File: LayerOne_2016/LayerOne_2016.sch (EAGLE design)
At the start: 63 parts, among them IC1 M74VHC1GT125DF2G, IC2 PQ1X331M2ZP-3V3-LDO-SOT-23-5, IC9 M74VHC1GT125DF2G

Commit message: 
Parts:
- added JP10, JP6, JP7, JP8, JP9: (no value), SparkFun-Connectors:PINHD-2X10
- added JP11, JP12, JP13: (no value), microbuilder:HEADER-1X10
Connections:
- net 3.3V: now also JP11.1, JP11.10, JP11.2, JP11.3, JP11.4, JP11.5, JP11.6, JP11.7, JP11.8, JP11.9
- net GND: now also JP12.1, JP12.10, JP12.2, JP12.3, JP12.4, JP12.5, JP12.6, JP12.7, JP12.8, JP12.9
- net VCC: now also JP13.1, JP13.10, JP13.2, JP13.3, JP13.4, JP13.5, JP13.6, JP13.7, JP13.8, JP13.9
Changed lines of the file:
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@@
 </part>
 <part name="GND13" library="SparkFun-Aesthetics" deviceset="GND" device=""/>
+<part name="JP6" library="SparkFun-Connectors" deviceset="PINHD-2X10" device=""/>
+<part name="JP7" library="SparkFun-Connectors" deviceset="PINHD-2X10" device=""/>
+<part name="JP8" library="SparkFun-Connectors" deviceset="PINHD-2X10" device=""/>
+<part name="JP9" library="SparkFun-Connectors" deviceset="PINHD-2X10" device=""/>
+<part name="JP10" library="SparkFun-Connectors" deviceset="PINHD-2X10" device=""/>
+<part name="JP11" library="microbuilder" deviceset="HEADER-1X10" device=""/>
+<part name="JP12" library="microbuilder" deviceset="HEADER-1X10" device=""/>
+<part name="JP13" library="microbuilder" deviceset="HEADER-1X10" device=""/>
+<part name="U$2" library="microbuilder" deviceset="GND" device=""/>
 </parts>
 <sheets>
@@
 </plain>
 <instances>
+<instance part="JP6" gate="A" x="-10.16" y="66.04"/>
+<instance part="JP7" gate="A" x="7.62" y="66.04"/>
+<instance part="JP8" gate="A" x="25.4" y="66.04"/>
+<instance part="JP9" gate="A" x="43.18" y="66.04"/>
+<instance part="JP10" gate="A" x="60.96" y="66.04"/>
+<instance part="JP11" gate="A" x="81.28" y="66.04"/>
+<instance part="JP12" gate="A" x="-25.4" y="63.5" rot="R180"/>
+<instance part="JP13" gate="A" x="99.06" y="66.04"/>
+<instance part="U$2" gate="G$1" x="-22.86" y="43.18"/>
 </instances>
 <busses>
 </busses>
 <nets>
+<net name="GND" class="0">
+<segment>
+<pinref part="JP12" gate="A" pin="10"/>
+<wire x1="-22.86" y1="76.2" x2="-22.86" y2="73.66" width="0.1524" layer="91"/>
+<pinref part="JP12" gate="A" pin="1"/>
+<wire x1="-22.86" y1="73.66" x2="-22.86" y2="71.12" width="0.1524" layer="91"/>
+<wire x1="-22.86" y1="71.12" x2="-22.86" y2="68.58" width="0.1524" layer="91"/>
+<wire x1="-22.86" y1="68.58" x2="-22.86" y2="66.04" width="0.1524" layer="91"/>
+<wire x1="-22.86" y1="66.04" x2="-22.86" y2="63.5" width="0.1524" layer="91"/>
+<wire x1="-22.86" y1="63.5" x2="-22.86" y2="60.96" width="0.1524" layer="91"/>
+<wire x1="-22.86" y1="60.96" x2="-22.86" y2="58.42" width="0.1524" layer="91"/>
+<wire x1="-22.86" y1="58.42" x2="-22.86" y2="55.88" width="0.1524" layer="91"/>
+<wire x1="-22.86" y1="55.88" x2="-22.86" y2="53.34" width="0.1524" layer="91"/>
+<wire x1="-22.86" y1="53.34" x2="-22.86" y2="45.72" width="0.1524" layer="91"/>
+<junction x="-22.86" y="53.34"/>
+<pinref part="JP12" gate="A" pin="2"/>
+<junction x="-22.86" y="55.88"/>
+<pinref part="JP12" gate="A" pin="3"/>
+<junction x="-22.86" y="58.42"/>
+<pinref part="JP12" gate="A" pin="4"/>
+<junction x="-22.86" y="60.96"/>
+<pinref part="JP12" gate="A" pin="5"/>
+<junction x="-22.86" y="63.5"/>
+<pinref part="JP12" gate="A" pin="6"/>
+<junction x="-22.86" y="66.04"/>
+<pinref part="JP12" gate="A" pin="7"/>
+<junction x="-22.86" y="68.58"/>
+<pinref part="JP12" gate="A" pin="8"/>
+<junction x="-22.86" y="71.12"/>
+<pinref part="JP12" gate="A" pin="9"/>
+<junction x="-22.86" y="73.66"/>
+<pinref part="U$2" gate="G$1" pin="GND"/>
+</segment>
+</net>
+<net name="3.3V" class="0">
+<segment>
+<pinref part="JP11" gate="A" pin="1"/>
+<wire x1="78.74" y1="76.2" x2="78.74" y2="73.66" width="0.1524" layer="91"/>
+<pinref part="JP11" gate="A" pin="2"/>
+<wire x1="78.74" y1="73.66" x2="78.74" y2="71.12" width="0.1524" layer="91"/>
+<junction x="78.74" y="73.66"/>
+<pinref part="JP11" gate="A" pin="3"/>
+<wire x1="78.74" y1="71.12" x2="78.74" y2="68.58" width="0.1524" layer="91"/>
+<junction x="78.74" y="71.12"/>
+<pinref part="JP11" gate="A" pin="4"/>
+<wire x1="78.74" y1="68.58" x2="78.74" y2="66.04" width="0.1524" layer="91"/>
+<junction x="78.74" y="68.58"/>
+<pinref part="JP11" gate="A" pin="5"/>
+<wire x1="78.74" y1="66.04" x2="78.74" y2="63.5" width="0.1524" layer="91"/>
+<junction x="78.74" y="66.04"/>
+<pinref part="JP11" gate="A" pin="6"/>
+<wire x1="78.74" y1="63.5" x2="78.74" y2="60.96" width="0.1524" layer="91"/>
+<junction x="78.74" y="63.5"/>
+<pinref part="JP11" gate="A" pin="7"/>
+<wire x1="78.74" y1="60.96" x2="78.74" y2="58.42" width="0.1524" layer="91"/>
+<junction x="78.74" y="60.96"/>
+<pinref part="JP11" gate="A" pin="8"/>
+<wire x1="78.74" y1="58.42" x2="78.74" y2="55.88" width="0.1524" layer="91"/>
+<junction x="78.74" y="58.42"/>
+<pinref part="JP11" gate="A" pin="9"/>
+<wire x1="78.74" y1="55.88" x2="78.74" y2="53.34" width="0.1524" layer="91"/>
+<junction x="78.74" y="55.88"/>
+<pinref part="JP11" gate="A" pin="10"/>
+<wire x1="78.74" y1="53.34" x2="78.74" y2="45.72" width="0.1524" layer="91"/>
+<junction x="78.74" y="53.34"/>
+<label x="78.74" y="43.18" size="1.778" layer="95"/>
+</segment>
+</net>
+<net name="VCC" class="0">
+<segment>
+<pinref part="JP13" gate="A" pin="1"/>
+<wire x1="96.52" y1="76.2" x2="96.52" y2="73.66" width="0.1524" layer="91"/>
+<pinref part="JP13" gate="A" pin="2"/>
+<wire x1="96.52" y1="73.66" x2="96.52" y2="71.12" width="0.1524" layer="91"/>
+<junction x="96.52" y="73.66"/>
+<pinref part="JP13" gate="A" pin="3"/>
+<wire x1="96.52" y1="71.12" x2="96.52" y2="68.58" width="0.1524" layer="91"/>
+<junction x="96.52" y="71.12"/>
+<pinref part="JP13" gate="A" pin="4"/>
+<wire x1="96.52" y1="68.58" x2="96.52" y2="66.04" width="0.1524" layer="91"/>
+<junction x="96.52" y="68.58"/>
+<pinref part="JP13" gate="A" pin="5"/>
+<wire x1="96.52" y1="66.04" x2="96.52" y2="63.5" width="0.1524" layer="91"/>
+<junction x="96.52" y="66.04"/>
+<pinref part="JP13" gate="A" pin="6"/>
+<wire x1="96.52" y1="63.5" x2="96.52" y2="60.96" width="0.1524" layer="91"/>
+<junction x="96.52" y="63.5"/>
+<pinref part="JP13" gate="A" pin="7"/>
+<wire x1="96.52" y1="60.96" x2="96.52" y2="58.42" width="0.1524" layer="91"/>
+<junction x="96.52" y="60.96"/>
+<pinref part="JP13" gate="A" pin="8"/>
+<wire x1="96.52" y1="58.42" x2="96.52" y2="55.88" width="0.1524" layer="91"/>
+<junction x="96.52" y="58.42"/>
+<pinref part="JP13" gate="A" pin="9"/>
+<wire x1="96.52" y1="55.88" x2="96.52" y2="53.34" width="0.1524" layer="91"/>
+<junction x="96.52" y="55.88"/>
+<pinref part="JP13" gate="A" pin="10"/>
+<wire x1="96.52" y1="53.34" x2="96.52" y2="45.72" width="0.1524" layer="91"/>
+<junction x="96.52" y="53.34"/>
+<label x="96.52" y="43.18" size="1.778" layer="95"/>
+</segment>
+</net>
 </nets>
 </sheet>

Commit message: 
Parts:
- removed C27, C29: 0.1uF, SparkFun-Capacitors:CAP0805
- removed C28, C30: 1.0uF, SparkFun-Capacitors:CAP0805
- removed IC2: PQ1X331M2ZP-3V3-LDO-SOT-23-5, STM32-PROX:PQ1X331M2ZP-3V3-LDO-SOT-23-5
- removed IC9: M74VHC1GT125DF2G, 74xx-little-de:74AHC1G125DCK
- added C7: 100uF, SparkFun-Capacitors:CAP0805
- added IC3: (no value), v-reg-3:LM1117
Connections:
- removed net N$24: C31.1, IC2.NR
- net 3.3V: now also C31.1, IC3.OUT; no longer C27.1, C28.1, C29.1, C30.1, IC2.VO
- net DIN: no longer IC9A.O
- net GND: now also C7.2, IC3.GND; no longer C27.2, C28.2, C29.2, C30.2, IC2.GND, IC9A.OE
- net P1_5_3V: no longer IC9A.I
- net VCC: now also C7.1, IC3.IN; no longer IC2.VC, IC2.VIN
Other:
- moved on the sheet: C31

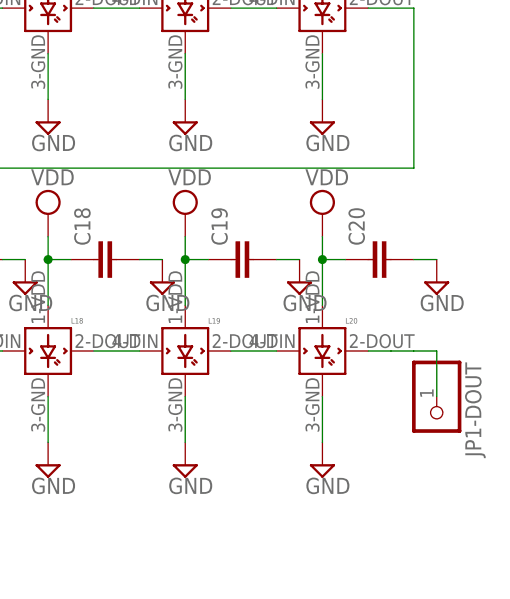
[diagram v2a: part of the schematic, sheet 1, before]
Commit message: 
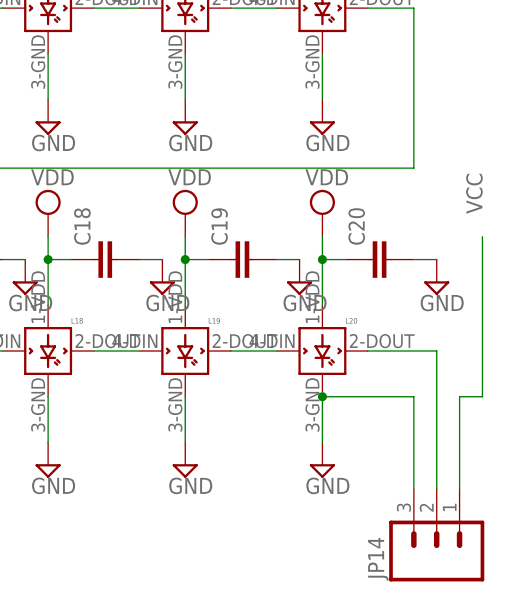
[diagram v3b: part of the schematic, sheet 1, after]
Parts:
- removed JP1-DOUT: (no value), adafruit:PINHD-1X1CB
- added JP14: (no value), SparkFun-Connectors:M031X03_NO_SILK
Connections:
- net GND: now also JP14.3
- net N$26: now also JP14.2; no longer JP1-DOUT.1
- net VCC: now also JP14.1
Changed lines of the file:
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@@
 <part name="SUPPLY21" library="supply2" deviceset="GND" device=""/>
 <part name="SUPPLY22" library="supply2" deviceset="GND" device=""/>
-<part name="JP1-DOUT" library="adafruit" deviceset="PINHD-1X1" device="CB"/>
 <part name="C2" library="SparkFun-Passives" deviceset="CAP" device="0805"/>
 <part name="SUPPLY25" library="supply2" deviceset="VDD" device=""/>
@@
 <part name="GND6" library="SparkFun-Aesthetics" deviceset="GND" device=""/>
 <part name="GND7" library="SparkFun-Aesthetics" deviceset="GND" device=""/>
+<part name="JP14" library="SparkFun-Connectors" deviceset="M03" device="1X03_NO_SILK"/>
 </parts>
 <sheets>
@@
 <instance part="SUPPLY21" gate="GND" x="124.46" y="27.94"/>
 <instance part="SUPPLY22" gate="GND" x="139.7" y="27.94"/>
-<instance part="JP1-DOUT" gate="G$1" x="152.4" y="33.02" rot="R270"/>
 <instance part="C2" gate="G$1" x="20.32" y="88.9" rot="R90"/>
 <instance part="SUPPLY25" gate="G$1" x="12.7" y="93.98"/>
@@
 <instance part="SUPPLY61" gate="G$1" x="139.7" y="55.88"/>
 <instance part="SUPPLY62" gate="GND" x="152.4" y="48.26"/>
+<instance part="JP14" gate="G$1" x="152.4" y="17.78" rot="R90"/>
 </instances>
 <busses>
@@
 <pinref part="SUPPLY22" gate="GND" pin="GND"/>
 <pinref part="L20" gate="G$1" pin="GND"/>
+<wire x1="139.7" y1="35.56" x2="149.86" y2="35.56" width="0.1524" layer="91"/>
+<pinref part="JP14" gate="G$1" pin="3"/>
+<wire x1="149.86" y1="35.56" x2="149.86" y2="25.4" width="0.1524" layer="91"/>
+<junction x="139.7" y="35.56"/>
 </segment>
 <segment>
@@
 <segment>
 <pinref part="L20" gate="G$1" pin="DOUT"/>
-<wire x1="144.78" y1="40.64" x2="147.32" y2="40.64" width="0.2032" layer="91"/>
-<wire x1="147.32" y1="40.64" x2="149.86" y2="40.64" width="0.2032" layer="91"/>
-<wire x1="149.86" y1="40.64" x2="152.4" y2="40.64" width="0.2032" layer="91"/>
-<wire x1="152.4" y1="40.64" x2="152.4" y2="35.56" width="0.2032" layer="91"/>
-<pinref part="JP1-DOUT" gate="G$1" pin="1"/>
+<wire x1="144.78" y1="40.64" x2="152.4" y2="40.64" width="0.2032" layer="91"/>
+<wire x1="152.4" y1="40.64" x2="152.4" y2="25.4" width="0.2032" layer="91"/>
+<pinref part="JP14" gate="G$1" pin="2"/>
 </segment>
 </net>
@@
 <pinref part="L20" gate="G$1" pin="VDD"/>
 </segment>
-</net>
+<segment>
+<pinref part="JP14" gate="G$1" pin="1"/>
+<wire x1="157.48" y1="35.56" x2="157.48" y2="53.34" width="0.2032" layer="91"/>
+<wire x1="157.48" y1="35.56" x2="154.94" y2="35.56" width="0.1524" layer="91"/>
+<wire x1="154.94" y1="35.56" x2="154.94" y2="25.4" width="0.1524" layer="91"/>
+<label x="157.48" y="55.88" size="1.778" layer="95" rot="R90"/>
+</segment>
+</net>
